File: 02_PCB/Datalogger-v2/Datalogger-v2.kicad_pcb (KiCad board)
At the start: 2 copper layers, 140 x 90 mm, 23 parts, among them U1 Micro SD Card Adapter, U7 TP4056, U8 ESP32 DEV KIT DOIT

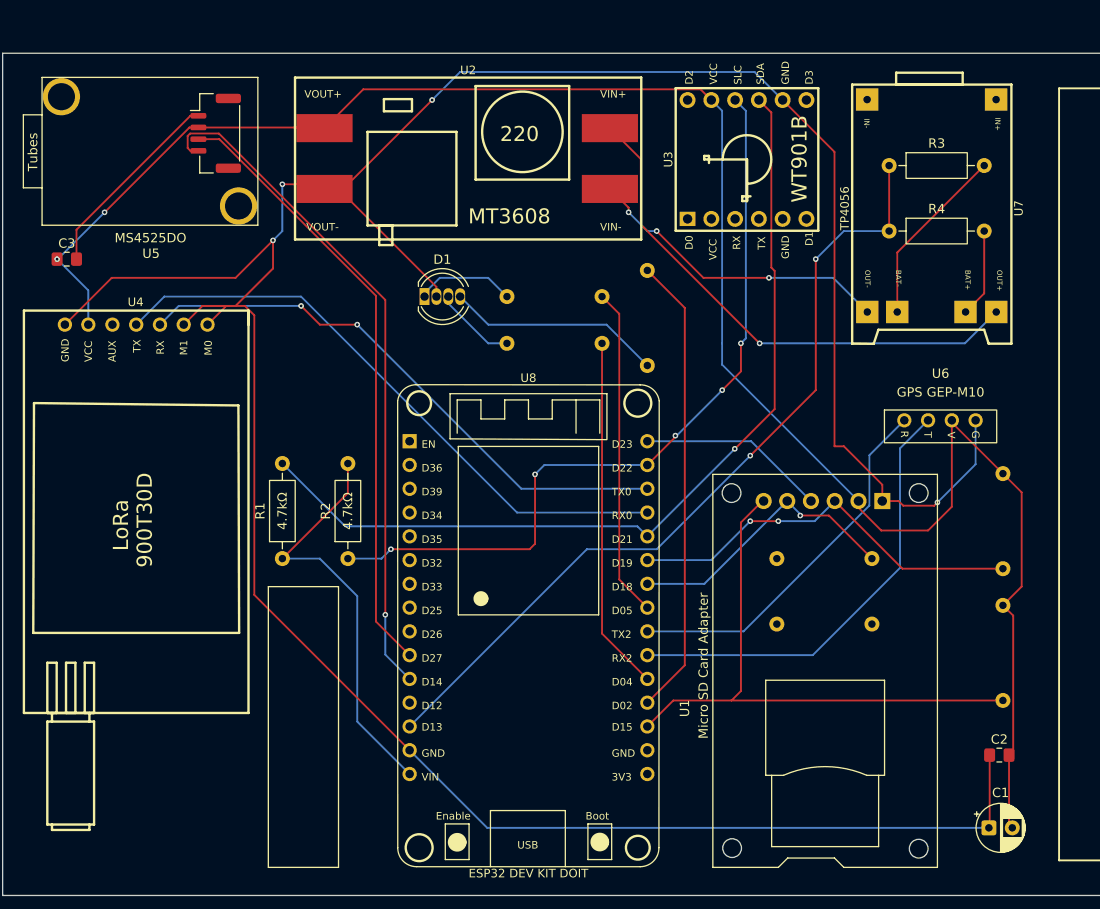
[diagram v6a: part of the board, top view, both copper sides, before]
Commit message: Update schematic and PCB layout
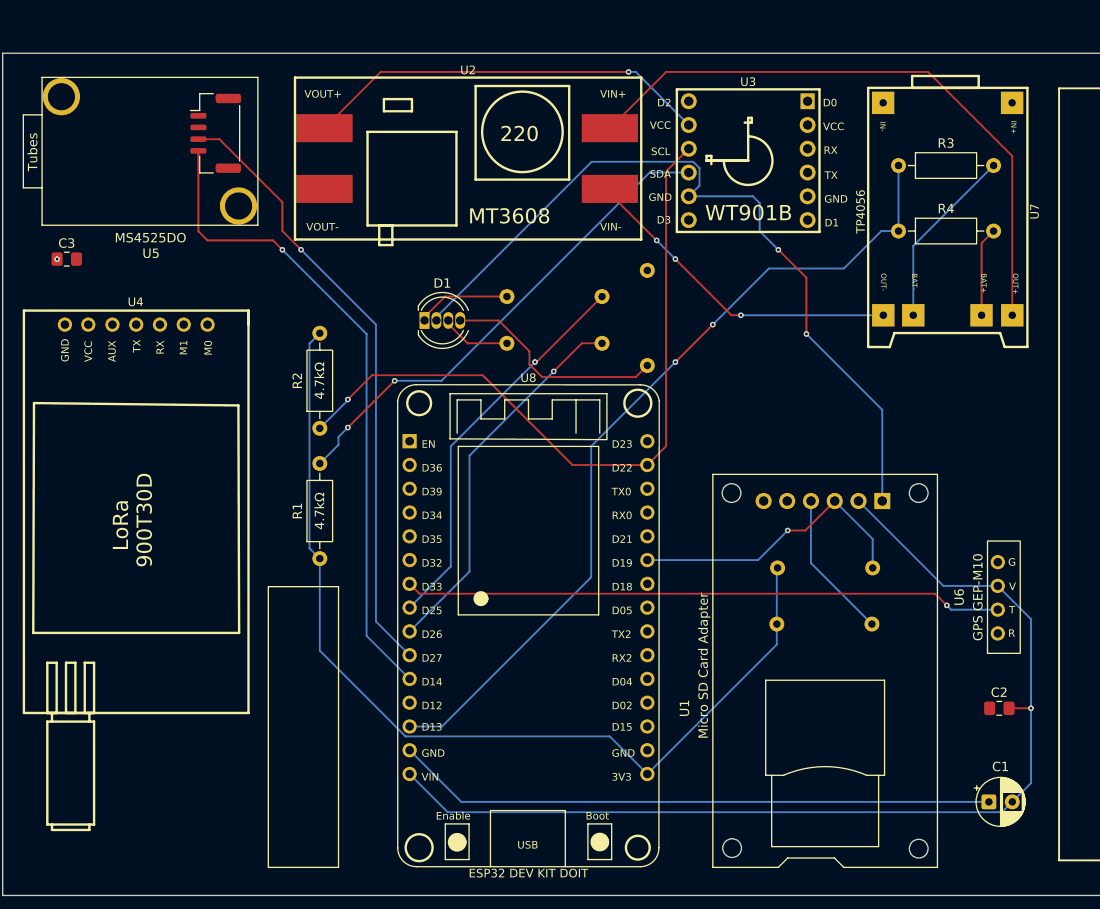
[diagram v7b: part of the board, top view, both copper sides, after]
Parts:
- removed R10, R11: 1kΩ, Resistor_THT:R_Axial_DIN0207_L6.3mm_D2.5mm_P10.16mm_Horizontal
- R3: value Resistor -> 2kΩ
- R4: value Resistor -> 560Ω
- R8, R9: value 1kΩ -> 4.7kΩ
- moved R9 26.1 mm to (211.9, 156.0), turned to 0 degrees
- moved U6 19.3 mm to (236.4, 159.1), turned to 90 degrees
- moved R2 14.2 mm to (163.0, 141.1)
- moved C2 5.00 mm to (235.6, 171.0)
- moved R1 4.00 mm to (163.0, 155.0)
- moved C1 2.77 mm to (234.5, 181.0)
- moved D1 2.55 mm to (174.2, 129.6)
- moved U7 1.75 mm to (229.6, 117.4)
- moved R3 1.00 mm to (224.8, 113.0)
- moved R4 1.00 mm to (224.8, 120.0)
- turned U3 to 0 degrees
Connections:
- C1 pad 2: 5V/2A -> +5V
- C2 pad 2: 5V/2A -> +5V
- C3 pad 1: 5V/2A -> +5V
- C3 pad 2: Net-(U5-GND) -> GND
- R1 pad 1: 5V/2A -> +3.3V
- R2 pad 2: 5V/2A -> +3.3V
- R5 pad 1: Net-(U8-LED0/D2) -> Net-(U8-ADC/D4)
- R6 pad 1: Net-(U8-ADC/D4) -> Net-(U8-ADC/DAC1/D26)
- R7 pad 1: Net-(U8-D5) -> Net-(U8-ADC/DAC0/D25)
- R8 pad 1: 5V/2A -> +3.3V
- R9 pad 1: 5V/2A -> +3.3V
- U1 pad 5: 5V/2A -> +5V
- U2 pad 3: 5V/2A -> +5V
- U3 pad 8: 5V/2A -> +5V
- U4 pad 6: 5V/2A -> +5V
- U5 pad 1: Net-(U5-GND) -> GND
- U5 pad 2: 5V/2A -> +5V
- U6 pad 3: 5V/2A -> +5V
- U8 pad 15: 5V/2A -> +5V
- U8 pad 18: Net-(U4-RX) -> unconnected-(U8-UA0TX/D1-Pad18)
- U8 pad 19: Net-(U4-TX) -> unconnected-(U8-UA0RX/D3-Pad19)
- U8 pad 23: Net-(U8-D5) -> Net-(U1-CS)
- U8 pad 24: Net-(U6-RX) -> Net-(U4-RX)
- U8 pad 25: Net-(U6-TX) -> Net-(U4-TX)
- U8 pad 27: Net-(U8-LED0/D2) -> unconnected-(U8-LED0/D2-Pad27)
- U8 pad 28: Net-(U1-CS) -> unconnected-(U8-ADC/D15-Pad28)
- U8 pad 29: (no net) -> unconnected-(U8-GND-Pad29)
- U8 pad 30: (no net) -> +3.3V
- U8 pad 6: unconnected-(U8-ADC/D32-Pad6) -> Net-(U6-RX)
- U8 pad 7: unconnected-(U8-ADC/D33-Pad7) -> Net-(U6-TX)
- U8 pad 8: unconnected-(U8-ADC/DAC0/D25-Pad8) -> Net-(U8-ADC/DAC0/D25)
- U8 pad 9: unconnected-(U8-ADC/DAC1/D26-Pad9) -> Net-(U8-ADC/DAC1/D26)
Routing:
- net 5V/2A: track 250.0 -> 0.00 mm, vias 2 -> 0
- net GND: track 324.7 -> 149.2 mm, vias 4 -> 2
- net +5V: track 0.00 -> 157.5 mm, vias 0 -> 3
- net +3.3V: track 0.00 -> 103.1 mm
- net Net-(U4-TX): track 65.4 -> 0.00 mm
- net Net-(U1-CS): track 62.0 -> 0.00 mm
- net Net-(U4-RX): track 61.0 -> 0.00 mm, vias 2 -> 0
- net Net-(U8-LED0/D2): track 49.5 -> 0.00 mm
- net Net-(U3-SDA): track 95.2 -> 52.8 mm, vias 1 -> 2
- net Net-(U8-ADC/DAC0/D25): track 0.00 -> 41.8 mm, vias 0 -> 1
- net Net-(U8-ADC/DAC1/D26): track 0.00 -> 40.6 mm, vias 0 -> 1
- net Net-(U6-RX): track 40.0 -> 0.00 mm
- net Net-(U8-ADC/D4): track 37.9 -> 0.00 mm
- net Net-(U8-D5): track 35.2 -> 0.00 mm
- net Net-(U1-SCK): track 30.4 -> 0.10 mm, vias 1 -> 0
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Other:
- board text added: "Keep in mind for LoRa: power routing must be avoided under the module (top or bottom layer)"
- board text removed: "Keep in mind for LoRa: power routing must be avoided under the module (top or bottom layer)."
- board text removed: "Next step: compare constraints of past Datalogger's PCB with this one. Just copy and paste the values. Specifically the vias holes?? (Just anything)"

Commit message: Upload schematic screenshot
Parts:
- moved R2 73.2 mm to (102.3, 100.1)
- moved C1 73.2 mm to (173.8, 140.0)
- moved C2 73.2 mm to (175.0, 130.0)
- moved C3 73.2 mm to (75.3, 82.0)
- moved R1 73.2 mm to (102.3, 114.0)
- moved R3 73.2 mm to (164.2, 72.0)
- moved R4 73.2 mm to (164.2, 79.0)
- moved R5 73.2 mm to (137.3, 83.2)
- moved R6 73.2 mm to (132.5, 91.0)
- moved R7 73.2 mm to (132.5, 86.0)
- moved R8 73.2 mm to (151.2, 121.0)
- moved U1 73.2 mm to (144.4, 147.0)
- moved U3 73.2 mm to (148.0, 71.5)
- moved U5 73.2 mm to (84.3, 85.0)
- moved U6 73.2 mm to (175.7, 118.1)
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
